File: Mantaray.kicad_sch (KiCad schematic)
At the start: 0 parts

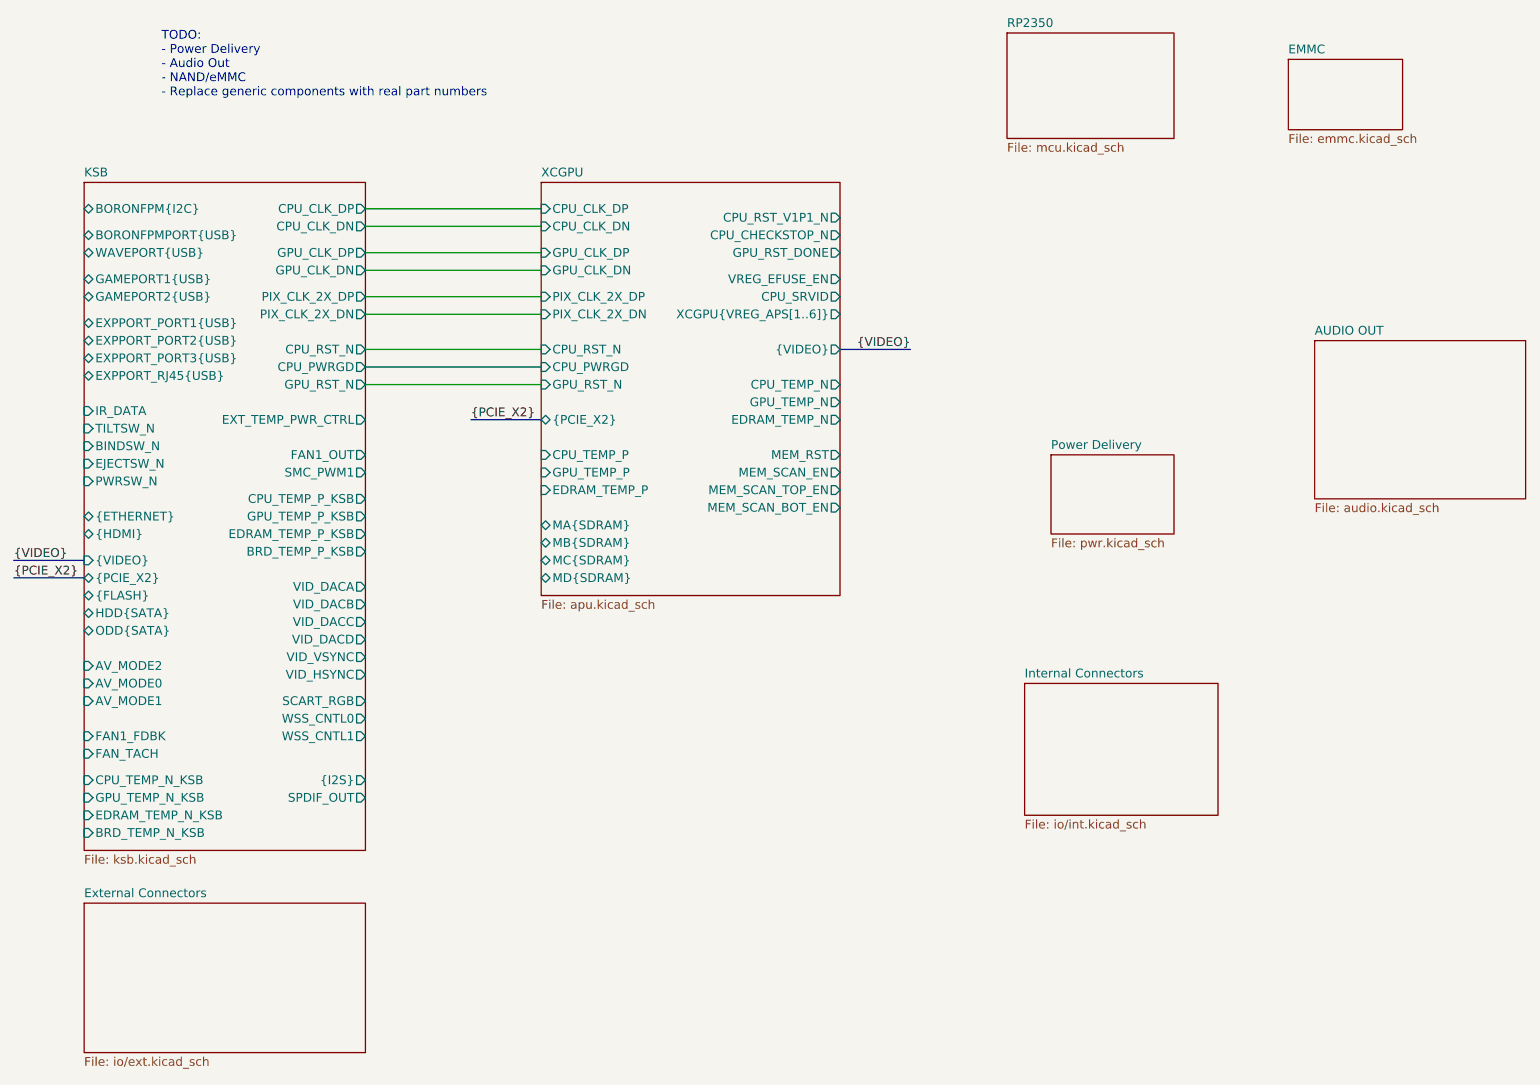
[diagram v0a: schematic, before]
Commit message: Add VRAM schematic
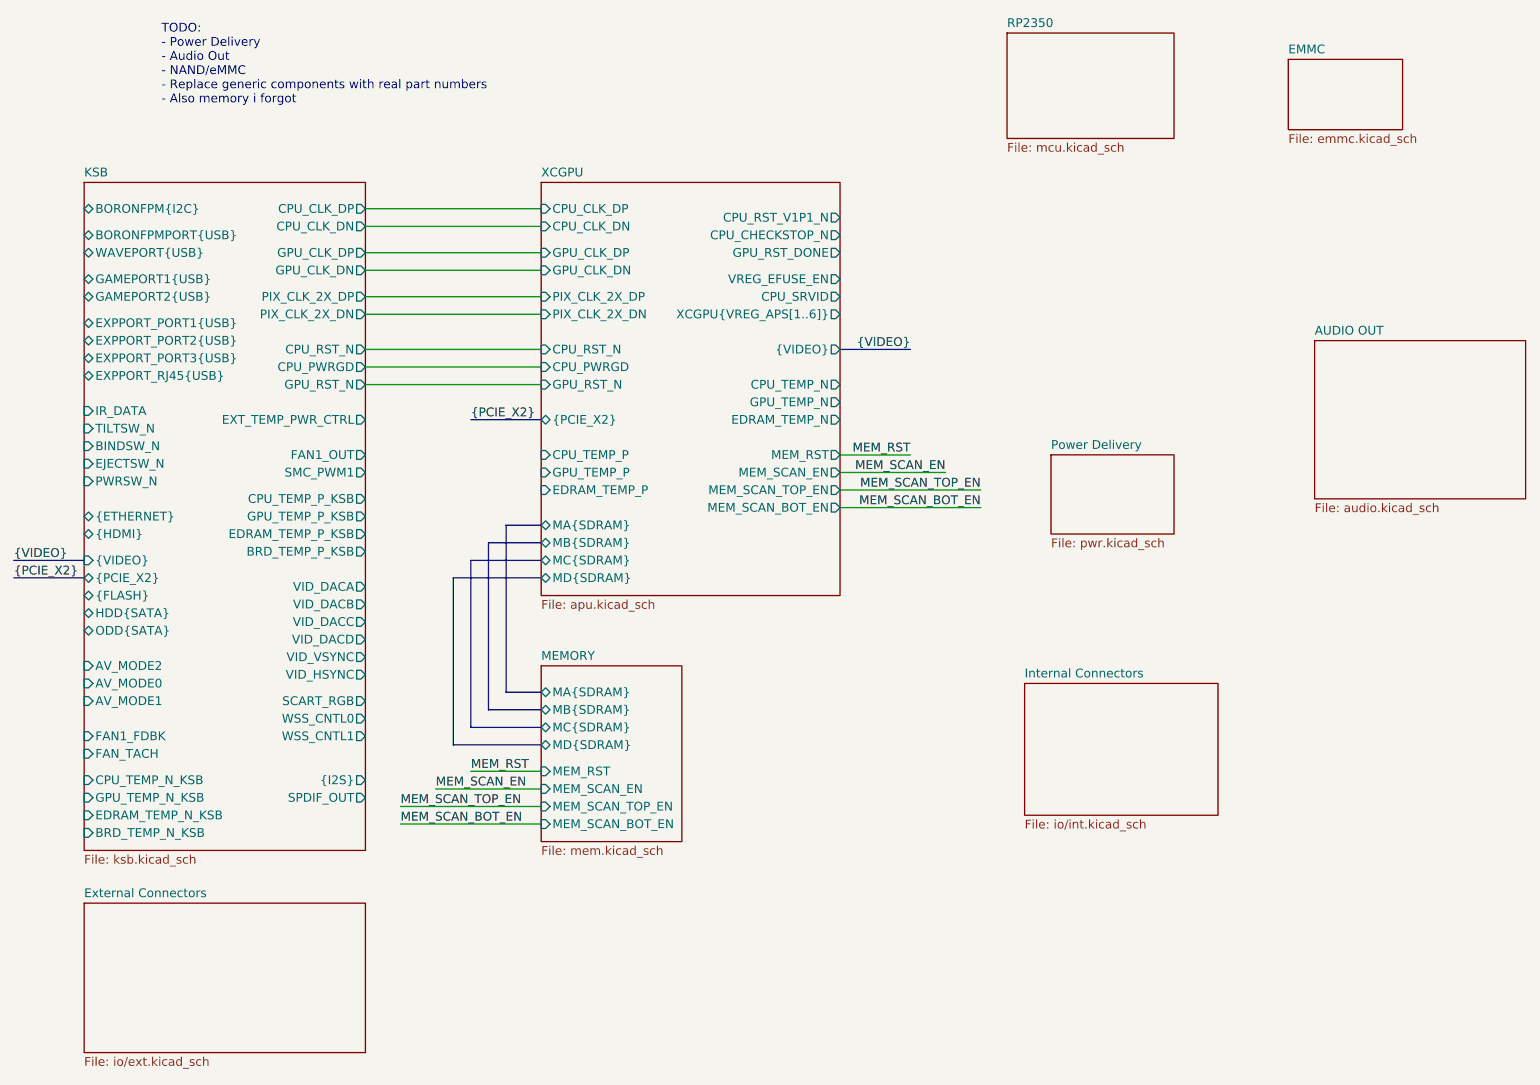
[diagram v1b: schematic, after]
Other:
- added sheet MEMORY (mem.kicad_sch)
- note added: "TODO: - Power Delivery - Audio Out - NAND/eMMC - Replace generic components with real part numbers - Also memory i forgot"
- note removed: "TODO: - Power Delivery - Audio Out - NAND/eMMC - Replace generic components with real part numbers"
